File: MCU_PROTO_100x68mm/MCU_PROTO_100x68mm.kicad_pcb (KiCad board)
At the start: 2 copper layers, 90 x 58 mm, 251 parts, among them J1 Screw_Terminal_01x03, J10 Conn_01x01_Male, J2 Screw_Terminal_01x03, J3 Conn_01x20_Female, J4 Conn_01x20_Female, J5 Conn_01x20_Female, J6 Conn_01x20_Female, J7 Conn_01x20_Female, J8 Conn_01x20_Female, J9 Conn_01x01_Male

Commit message: pads in process
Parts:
- removed the REF** at (157.5, 143.6)
- removed the REF** at (134.7, 143.6)
- removed the REF** at (139.7, 118.2)
- removed the REF** at (137.2, 118.2)
- removed the REF** at (134.7, 118.2)
- removed the REF** at (132.1, 118.2)
- removed the REF** at (129.6, 118.2)
- removed the REF** at (127.0, 118.2)
- removed the REF** at (124.5, 118.2)
- removed the REF** at (122.0, 118.2)
- removed the REF** at (119.4, 118.2)
- removed the REF** at (116.9, 118.2)
- removed the REF** at (132.1, 143.6)
- removed the REF** at (114.3, 118.2)
- removed the REF** at (111.8, 118.2)
- removed the REF** at (109.3, 118.2)
- removed the REF** at (157.5, 115.6)
- removed the REF** at (155.0, 115.6)
- removed the REF** at (152.4, 115.6)
- removed the REF** at (149.9, 115.6)
- removed the REF** at (147.4, 115.6)
- removed the REF** at (144.8, 115.6)
- removed the REF** at (142.3, 115.6)
- removed the REF** at (129.6, 143.6)
- removed the REF** at (139.7, 115.6)
- removed the REF** at (137.2, 115.6)
- removed the REF** at (134.7, 115.6)
- removed the REF** at (132.1, 115.6)
- removed the REF** at (129.6, 115.6)
- removed the REF** at (127.0, 115.6)
- removed the REF** at (124.5, 115.6)
- removed the REF** at (122.0, 115.6)
- removed the REF** at (119.4, 115.6)
- removed the REF** at (116.9, 115.6)
- removed the REF** at (127.0, 143.6)
- removed the REF** at (114.3, 115.6)
- removed the REF** at (111.8, 115.6)
- removed the REF** at (109.3, 115.6)
- removed the REF** at (157.5, 113.1)
- removed the REF** at (155.0, 113.1)
- removed the REF** at (152.4, 113.1)
- removed the REF** at (149.9, 113.1)
- removed the REF** at (147.4, 113.1)
- removed the REF** at (144.8, 113.1)
- removed the REF** at (142.3, 113.1)
- removed the REF** at (124.5, 143.6)
- removed the REF** at (139.7, 113.1)
- removed the REF** at (137.2, 113.1)
- removed the REF** at (134.7, 113.1)
- removed the REF** at (132.1, 113.1)
- removed the REF** at (129.6, 113.1)
- removed the REF** at (127.0, 113.1)
- removed the REF** at (124.5, 113.1)
- removed the REF** at (122.0, 113.1)
- removed the REF** at (119.4, 113.1)
- removed the REF** at (116.9, 113.1)
- removed the REF** at (122.0, 143.6)
- removed the REF** at (114.3, 113.1)
- removed the REF** at (111.8, 113.1)
- removed the REF** at (109.3, 113.1)
- removed the REF** at (157.5, 110.5)
- removed the REF** at (155.0, 110.5)
- removed the REF** at (152.4, 110.5)
- removed the REF** at (149.9, 110.5)
- removed the REF** at (147.4, 110.5)
- removed the REF** at (144.8, 110.5)
- removed the REF** at (142.3, 110.5)
- removed the REF** at (119.4, 143.6)
- removed the REF** at (139.7, 110.5)
- removed the REF** at (137.2, 110.5)
- removed the REF** at (134.7, 110.5)
- removed the REF** at (132.1, 110.5)
- removed the REF** at (129.6, 110.5)
- removed the REF** at (127.0, 110.5)
- removed the REF** at (124.5, 110.5)
- removed the REF** at (122.0, 110.5)
- removed the REF** at (119.4, 110.5)
- removed the REF** at (116.9, 110.5)
- removed the REF** at (157.5, 141.0)
- removed the REF** at (114.3, 110.5)
- removed the REF** at (111.8, 110.5)
- removed the REF** at (109.3, 110.5)
- removed the REF** at (157.5, 108.0)
- removed the REF** at (155.0, 108.0)
- removed the REF** at (152.4, 108.0)
- removed the REF** at (149.9, 108.0)
- removed the REF** at (147.4, 108.0)
- removed the REF** at (144.8, 108.0)
- removed the REF** at (142.3, 108.0)
- removed the REF** at (155.0, 141.0)
- removed the REF** at (139.7, 108.0)
- removed the REF** at (137.2, 108.0)
- removed the REF** at (134.7, 108.0)
- removed the REF** at (132.1, 108.0)
- removed the REF** at (129.6, 108.0)
- removed the REF** at (127.0, 108.0)
- removed the REF** at (124.5, 108.0)
- removed the REF** at (122.0, 108.0)
- removed the REF** at (119.4, 108.0)
- removed the REF** at (116.9, 108.0)
- removed the REF** at (152.4, 141.0)
- removed the REF** at (114.3, 108.0)
- removed the REF** at (111.8, 108.0)
- removed the REF** at (122.0, 146.1)
- removed the REF** at (155.0, 143.6)
- removed the REF** at (149.9, 141.0)
- removed the REF** at (119.4, 146.1)
- removed the REF** at (157.5, 146.1)
- removed the REF** at (155.0, 146.1)
- removed the REF** at (137.2, 146.1)
- removed the REF** at (144.8, 146.1)
- removed the REF** at (139.7, 146.1)
- removed the REF** at (134.7, 146.1)
- removed the REF** at (132.1, 146.1)
- removed the REF** at (129.6, 146.1)
- removed the REF** at (127.0, 146.1)
- removed the REF** at (147.4, 141.0)
- removed the REF** at (124.5, 146.1)
- removed the REF** at (142.3, 146.1)
- removed the REF** at (147.4, 146.1)
- removed the REF** at (152.4, 146.1)
- removed the REF** at (149.9, 146.1)
- removed the REF** at (144.8, 141.0)
- removed the REF** at (160.1, 114.7)
- removed the REF** at (160.1, 137.8)
- removed the REF** at (160.1, 134.3)
- removed the REF** at (160.1, 130.8)
- removed the REF** at (160.1, 118.2)
- removed the REF** at (160.1, 111.2)
- removed the REF** at (142.3, 141.0)
- removed the REF** at (139.7, 141.0)
- removed the REF** at (137.2, 141.0)
- removed the REF** at (134.7, 141.0)
- removed the REF** at (132.1, 141.0)
- removed the REF** at (129.6, 141.0)
- removed the REF** at (127.0, 141.0)
- removed the REF** at (152.4, 143.6)
- removed the REF** at (124.5, 141.0)
- removed the REF** at (122.0, 141.0)
- removed the REF** at (119.4, 141.0)
- removed the REF** at (157.5, 138.5)
- removed the REF** at (155.0, 138.5)
- removed the REF** at (152.4, 138.5)
- removed the REF** at (149.9, 138.5)
- removed the REF** at (147.4, 138.5)
- removed the REF** at (144.8, 138.5)
- removed the REF** at (142.3, 138.5)
- removed the REF** at (149.9, 143.6)
- removed the REF** at (139.7, 138.5)
- removed the REF** at (137.2, 138.5)
- removed the REF** at (134.7, 138.5)
- removed the REF** at (132.1, 138.5)
- removed the REF** at (129.6, 138.5)
- removed the REF** at (127.0, 138.5)
- removed the REF** at (124.5, 138.5)
- removed the REF** at (122.0, 138.5)
- removed the REF** at (119.4, 138.5)
- removed the REF** at (116.9, 138.5)
- removed the REF** at (147.4, 143.6)
- removed the REF** at (114.3, 138.5)
- removed the REF** at (111.8, 138.5)
- removed the REF** at (109.3, 138.5)
- removed the REF** at (157.5, 135.9)
- removed the REF** at (155.0, 135.9)
- removed the REF** at (152.4, 135.9)
- removed the REF** at (149.9, 135.9)
- removed the REF** at (147.4, 135.9)
- removed the REF** at (144.8, 135.9)
- removed the REF** at (142.3, 135.9)
- removed the REF** at (144.8, 143.6)
- removed the REF** at (139.7, 135.9)
- removed the REF** at (137.2, 135.9)
- removed the REF** at (134.7, 135.9)
- removed the REF** at (132.1, 135.9)
- removed the REF** at (129.6, 135.9)
- removed the REF** at (127.0, 135.9)
- removed the REF** at (124.5, 135.9)
- removed the REF** at (122.0, 135.9)
- removed the REF** at (119.4, 135.9)
- removed the REF** at (116.9, 135.9)
- removed the REF** at (142.3, 143.6)
- removed the REF** at (114.3, 135.9)
- removed the REF** at (111.8, 135.9)
- removed the REF** at (157.5, 120.7)
- removed the REF** at (155.0, 120.7)
- removed the REF** at (152.4, 120.7)
- removed the REF** at (149.9, 120.7)
- removed the REF** at (147.4, 120.7)
- removed the REF** at (144.8, 120.7)
- removed the REF** at (142.3, 120.7)
- removed the REF** at (139.7, 143.6)
- removed the REF** at (139.7, 120.7)
- removed the REF** at (137.2, 120.7)
- removed the REF** at (134.7, 120.7)
- removed the REF** at (132.1, 120.7)
- removed the REF** at (129.6, 120.7)
- removed the REF** at (127.0, 120.7)
- removed the REF** at (124.5, 120.7)
- removed the REF** at (122.0, 120.7)
- removed the REF** at (119.4, 120.7)
- removed the REF** at (116.9, 120.7)
- removed the REF** at (137.2, 143.6)
- removed the REF** at (114.3, 120.7)
- removed the REF** at (111.8, 120.7)
- removed the REF** at (109.3, 120.7)
- removed the REF** at (157.5, 118.2)
- removed the REF** at (155.0, 118.2)
- removed the REF** at (152.4, 118.2)
- removed the REF** at (149.9, 118.2)
- removed the REF** at (147.4, 118.2)
- removed the REF** at (144.8, 118.2)
- removed the REF** at (142.3, 118.2)
- added REF**: SolderWirePad_1x01_Drill0.8mm, Connector_Wire:SolderWirePad_1x01_Drill0.8mm, F.Cu at (161.3, 146.1)
- added REF**: SolderWirePad_1x01_Drill0.8mm, Connector_Wire:SolderWirePad_1x01_Drill0.8mm, F.Cu at (138.4, 146.1)
- added REF**: SolderWirePad_1x01_Drill0.8mm, Connector_Wire:SolderWirePad_1x01_Drill0.8mm, F.Cu at (161.3, 120.7)
- added REF**: SolderWirePad_1x01_Drill0.8mm, Connector_Wire:SolderWirePad_1x01_Drill0.8mm, F.Cu at (158.7, 120.7)
- added REF**: SolderWirePad_1x01_Drill0.8mm, Connector_Wire:SolderWirePad_1x01_Drill0.8mm, F.Cu at (156.2, 120.7)
- added REF**: SolderWirePad_1x01_Drill0.8mm, Connector_Wire:SolderWirePad_1x01_Drill0.8mm, F.Cu at (153.6, 120.7)
- added REF**: SolderWirePad_1x01_Drill0.8mm, Connector_Wire:SolderWirePad_1x01_Drill0.8mm, F.Cu at (151.1, 120.7)
- added REF**: SolderWirePad_1x01_Drill0.8mm, Connector_Wire:SolderWirePad_1x01_Drill0.8mm, F.Cu at (148.6, 120.7)
- added REF**: SolderWirePad_1x01_Drill0.8mm, Connector_Wire:SolderWirePad_1x01_Drill0.8mm, F.Cu at (146.0, 120.7)
- added REF**: SolderWirePad_1x01_Drill0.8mm, Connector_Wire:SolderWirePad_1x01_Drill0.8mm, F.Cu at (143.5, 120.7)
- added REF**: SolderWirePad_1x01_Drill0.8mm, Connector_Wire:SolderWirePad_1x01_Drill0.8mm, F.Cu at (140.9, 120.7)
- added REF**: SolderWirePad_1x01_Drill0.8mm, Connector_Wire:SolderWirePad_1x01_Drill0.8mm, F.Cu at (138.4, 120.7)
- added REF**: SolderWirePad_1x01_Drill0.8mm, Connector_Wire:SolderWirePad_1x01_Drill0.8mm, F.Cu at (135.9, 146.1)
- added REF**: SolderWirePad_1x01_Drill0.8mm, Connector_Wire:SolderWirePad_1x01_Drill0.8mm, F.Cu at (135.9, 120.7)
- added REF**: SolderWirePad_1x01_Drill0.8mm, Connector_Wire:SolderWirePad_1x01_Drill0.8mm, F.Cu at (133.3, 120.7)
- added REF**: SolderWirePad_1x01_Drill0.8mm, Connector_Wire:SolderWirePad_1x01_Drill0.8mm, F.Cu at (130.8, 120.7)
- added REF**: SolderWirePad_1x01_Drill0.8mm, Connector_Wire:SolderWirePad_1x01_Drill0.8mm, F.Cu at (128.2, 120.7)
- added REF**: SolderWirePad_1x01_Drill0.8mm, Connector_Wire:SolderWirePad_1x01_Drill0.8mm, F.Cu at (125.7, 120.7)
- added REF**: SolderWirePad_1x01_Drill0.8mm, Connector_Wire:SolderWirePad_1x01_Drill0.8mm, F.Cu at (123.2, 120.7)
- added REF**: SolderWirePad_1x01_Drill0.8mm, Connector_Wire:SolderWirePad_1x01_Drill0.8mm, F.Cu at (120.6, 120.7)
- added REF**: SolderWirePad_1x01_Drill0.8mm, Connector_Wire:SolderWirePad_1x01_Drill0.8mm, F.Cu at (118.1, 120.7)
- added REF**: SolderWirePad_1x01_Drill0.8mm, Connector_Wire:SolderWirePad_1x01_Drill0.8mm, F.Cu at (115.5, 120.7)
- added REF**: SolderWirePad_1x01_Drill0.8mm, Connector_Wire:SolderWirePad_1x01_Drill0.8mm, F.Cu at (113.0, 120.7)
- added REF**: SolderWirePad_1x01_Drill0.8mm, Connector_Wire:SolderWirePad_1x01_Drill0.8mm, F.Cu at (133.3, 146.1)
- added REF**: SolderWirePad_1x01_Drill0.8mm, Connector_Wire:SolderWirePad_1x01_Drill0.8mm, F.Cu at (161.3, 118.2)
- added REF**: SolderWirePad_1x01_Drill0.8mm, Connector_Wire:SolderWirePad_1x01_Drill0.8mm, F.Cu at (158.7, 118.2)
- added REF**: SolderWirePad_1x01_Drill0.8mm, Connector_Wire:SolderWirePad_1x01_Drill0.8mm, F.Cu at (156.2, 118.2)
- added REF**: SolderWirePad_1x01_Drill0.8mm, Connector_Wire:SolderWirePad_1x01_Drill0.8mm, F.Cu at (153.6, 118.2)
- added REF**: SolderWirePad_1x01_Drill0.8mm, Connector_Wire:SolderWirePad_1x01_Drill0.8mm, F.Cu at (151.1, 118.2)
- added REF**: SolderWirePad_1x01_Drill0.8mm, Connector_Wire:SolderWirePad_1x01_Drill0.8mm, F.Cu at (148.6, 118.2)
- added REF**: SolderWirePad_1x01_Drill0.8mm, Connector_Wire:SolderWirePad_1x01_Drill0.8mm, F.Cu at (146.0, 118.2)
- added REF**: SolderWirePad_1x01_Drill0.8mm, Connector_Wire:SolderWirePad_1x01_Drill0.8mm, F.Cu at (143.5, 118.2)
- added REF**: SolderWirePad_1x01_Drill0.8mm, Connector_Wire:SolderWirePad_1x01_Drill0.8mm, F.Cu at (140.9, 118.2)
- added REF**: SolderWirePad_1x01_Drill0.8mm, Connector_Wire:SolderWirePad_1x01_Drill0.8mm, F.Cu at (138.4, 118.2)
- added REF**: SolderWirePad_1x01_Drill0.8mm, Connector_Wire:SolderWirePad_1x01_Drill0.8mm, F.Cu at (130.8, 146.1)
- added REF**: SolderWirePad_1x01_Drill0.8mm, Connector_Wire:SolderWirePad_1x01_Drill0.8mm, F.Cu at (135.9, 118.2)
- added REF**: SolderWirePad_1x01_Drill0.8mm, Connector_Wire:SolderWirePad_1x01_Drill0.8mm, F.Cu at (133.3, 118.2)
- added REF**: SolderWirePad_1x01_Drill0.8mm, Connector_Wire:SolderWirePad_1x01_Drill0.8mm, F.Cu at (130.8, 118.2)
- added REF**: SolderWirePad_1x01_Drill0.8mm, Connector_Wire:SolderWirePad_1x01_Drill0.8mm, F.Cu at (128.2, 118.2)
- added REF**: SolderWirePad_1x01_Drill0.8mm, Connector_Wire:SolderWirePad_1x01_Drill0.8mm, F.Cu at (125.7, 118.2)
- added REF**: SolderWirePad_1x01_Drill0.8mm, Connector_Wire:SolderWirePad_1x01_Drill0.8mm, F.Cu at (123.2, 118.2)
- added REF**: SolderWirePad_1x01_Drill0.8mm, Connector_Wire:SolderWirePad_1x01_Drill0.8mm, F.Cu at (120.6, 118.2)
- added REF**: SolderWirePad_1x01_Drill0.8mm, Connector_Wire:SolderWirePad_1x01_Drill0.8mm, F.Cu at (118.1, 118.2)
- added REF**: SolderWirePad_1x01_Drill0.8mm, Connector_Wire:SolderWirePad_1x01_Drill0.8mm, F.Cu at (115.5, 118.2)
- added REF**: SolderWirePad_1x01_Drill0.8mm, Connector_Wire:SolderWirePad_1x01_Drill0.8mm, F.Cu at (113.0, 118.2)
- added REF**: SolderWirePad_1x01_Drill0.8mm, Connector_Wire:SolderWirePad_1x01_Drill0.8mm, F.Cu at (128.2, 146.1)
- added REF**: SolderWirePad_1x01_Drill0.8mm, Connector_Wire:SolderWirePad_1x01_Drill0.8mm, F.Cu at (161.3, 115.6)
- added REF**: SolderWirePad_1x01_Drill0.8mm, Connector_Wire:SolderWirePad_1x01_Drill0.8mm, F.Cu at (158.7, 115.6)
- added REF**: SolderWirePad_1x01_Drill0.8mm, Connector_Wire:SolderWirePad_1x01_Drill0.8mm, F.Cu at (156.2, 115.6)
- added REF**: SolderWirePad_1x01_Drill0.8mm, Connector_Wire:SolderWirePad_1x01_Drill0.8mm, F.Cu at (153.6, 115.6)
- added REF**: SolderWirePad_1x01_Drill0.8mm, Connector_Wire:SolderWirePad_1x01_Drill0.8mm, F.Cu at (151.1, 115.6)
- added REF**: SolderWirePad_1x01_Drill0.8mm, Connector_Wire:SolderWirePad_1x01_Drill0.8mm, F.Cu at (148.6, 115.6)
- added REF**: SolderWirePad_1x01_Drill0.8mm, Connector_Wire:SolderWirePad_1x01_Drill0.8mm, F.Cu at (146.0, 115.6)
- added REF**: SolderWirePad_1x01_Drill0.8mm, Connector_Wire:SolderWirePad_1x01_Drill0.8mm, F.Cu at (143.5, 115.6)
- added REF**: SolderWirePad_1x01_Drill0.8mm, Connector_Wire:SolderWirePad_1x01_Drill0.8mm, F.Cu at (140.9, 115.6)
- added REF**: SolderWirePad_1x01_Drill0.8mm, Connector_Wire:SolderWirePad_1x01_Drill0.8mm, F.Cu at (138.4, 115.6)
- added REF**: SolderWirePad_1x01_Drill0.8mm, Connector_Wire:SolderWirePad_1x01_Drill0.8mm, F.Cu at (125.7, 146.1)
- added REF**: SolderWirePad_1x01_Drill0.8mm, Connector_Wire:SolderWirePad_1x01_Drill0.8mm, F.Cu at (135.9, 115.6)
- added REF**: SolderWirePad_1x01_Drill0.8mm, Connector_Wire:SolderWirePad_1x01_Drill0.8mm, F.Cu at (133.3, 115.6)
- added REF**: SolderWirePad_1x01_Drill0.8mm, Connector_Wire:SolderWirePad_1x01_Drill0.8mm, F.Cu at (130.8, 115.6)
- added REF**: SolderWirePad_1x01_Drill0.8mm, Connector_Wire:SolderWirePad_1x01_Drill0.8mm, F.Cu at (128.2, 115.6)
- added REF**: SolderWirePad_1x01_Drill0.8mm, Connector_Wire:SolderWirePad_1x01_Drill0.8mm, F.Cu at (125.7, 115.6)
- added REF**: SolderWirePad_1x01_Drill0.8mm, Connector_Wire:SolderWirePad_1x01_Drill0.8mm, F.Cu at (123.2, 115.6)
- added REF**: SolderWirePad_1x01_Drill0.8mm, Connector_Wire:SolderWirePad_1x01_Drill0.8mm, F.Cu at (120.6, 115.6)
- added REF**: SolderWirePad_1x01_Drill0.8mm, Connector_Wire:SolderWirePad_1x01_Drill0.8mm, F.Cu at (118.1, 115.6)
- added REF**: SolderWirePad_1x01_Drill0.8mm, Connector_Wire:SolderWirePad_1x01_Drill0.8mm, F.Cu at (115.5, 115.6)
- added REF**: SolderWirePad_1x01_Drill0.8mm, Connector_Wire:SolderWirePad_1x01_Drill0.8mm, F.Cu at (113.0, 115.6)
- added REF**: SolderWirePad_1x01_Drill0.8mm, Connector_Wire:SolderWirePad_1x01_Drill0.8mm, F.Cu at (123.2, 146.1)
- added REF**: SolderWirePad_1x01_Drill0.8mm, Connector_Wire:SolderWirePad_1x01_Drill0.8mm, F.Cu at (161.3, 113.1)
- added REF**: SolderWirePad_1x01_Drill0.8mm, Connector_Wire:SolderWirePad_1x01_Drill0.8mm, F.Cu at (158.7, 113.1)
- added REF**: SolderWirePad_1x01_Drill0.8mm, Connector_Wire:SolderWirePad_1x01_Drill0.8mm, F.Cu at (156.2, 113.1)
- added REF**: SolderWirePad_1x01_Drill0.8mm, Connector_Wire:SolderWirePad_1x01_Drill0.8mm, F.Cu at (153.6, 113.1)
- added REF**: SolderWirePad_1x01_Drill0.8mm, Connector_Wire:SolderWirePad_1x01_Drill0.8mm, F.Cu at (151.1, 113.1)
- added REF**: SolderWirePad_1x01_Drill0.8mm, Connector_Wire:SolderWirePad_1x01_Drill0.8mm, F.Cu at (148.6, 113.1)
- added REF**: SolderWirePad_1x01_Drill0.8mm, Connector_Wire:SolderWirePad_1x01_Drill0.8mm, F.Cu at (146.0, 113.1)
- added REF**: SolderWirePad_1x01_Drill0.8mm, Connector_Wire:SolderWirePad_1x01_Drill0.8mm, F.Cu at (143.5, 113.1)
- added REF**: SolderWirePad_1x01_Drill0.8mm, Connector_Wire:SolderWirePad_1x01_Drill0.8mm, F.Cu at (140.9, 113.1)
- added REF**: SolderWirePad_1x01_Drill0.8mm, Connector_Wire:SolderWirePad_1x01_Drill0.8mm, F.Cu at (138.4, 113.1)
- added REF**: SolderWirePad_1x01_Drill0.8mm, Connector_Wire:SolderWirePad_1x01_Drill0.8mm, F.Cu at (120.6, 146.1)
- added REF**: SolderWirePad_1x01_Drill0.8mm, Connector_Wire:SolderWirePad_1x01_Drill0.8mm, F.Cu at (135.9, 113.1)
- added REF**: SolderWirePad_1x01_Drill0.8mm, Connector_Wire:SolderWirePad_1x01_Drill0.8mm, F.Cu at (133.3, 113.1)
- added REF**: SolderWirePad_1x01_Drill0.8mm, Connector_Wire:SolderWirePad_1x01_Drill0.8mm, F.Cu at (130.8, 113.1)
- added REF**: SolderWirePad_1x01_Drill0.8mm, Connector_Wire:SolderWirePad_1x01_Drill0.8mm, F.Cu at (128.2, 113.1)
- added REF**: SolderWirePad_1x01_Drill0.8mm, Connector_Wire:SolderWirePad_1x01_Drill0.8mm, F.Cu at (125.7, 113.1)
- added REF**: SolderWirePad_1x01_Drill0.8mm, Connector_Wire:SolderWirePad_1x01_Drill0.8mm, F.Cu at (123.2, 113.1)
- added REF**: SolderWirePad_1x01_Drill0.8mm, Connector_Wire:SolderWirePad_1x01_Drill0.8mm, F.Cu at (120.6, 113.1)
- added REF**: SolderWirePad_1x01_Drill0.8mm, Connector_Wire:SolderWirePad_1x01_Drill0.8mm, F.Cu at (118.1, 113.1)
- added REF**: SolderWirePad_1x01_Drill0.8mm, Connector_Wire:SolderWirePad_1x01_Drill0.8mm, F.Cu at (115.5, 113.1)
- added REF**: SolderWirePad_1x01_Drill0.8mm, Connector_Wire:SolderWirePad_1x01_Drill0.8mm, F.Cu at (113.0, 113.1)
- added REF**: SolderWirePad_1x01_Drill0.8mm, Connector_Wire:SolderWirePad_1x01_Drill0.8mm, F.Cu at (118.1, 146.1)
- added REF**: SolderWirePad_1x01_Drill0.8mm, Connector_Wire:SolderWirePad_1x01_Drill0.8mm, F.Cu at (161.3, 110.5)
- added REF**: SolderWirePad_1x01_Drill0.8mm, Connector_Wire:SolderWirePad_1x01_Drill0.8mm, F.Cu at (158.7, 110.5)
- added REF**: SolderWirePad_1x01_Drill0.8mm, Connector_Wire:SolderWirePad_1x01_Drill0.8mm, F.Cu at (156.2, 110.5)
- added REF**: SolderWirePad_1x01_Drill0.8mm, Connector_Wire:SolderWirePad_1x01_Drill0.8mm, F.Cu at (153.6, 110.5)
- added REF**: SolderWirePad_1x01_Drill0.8mm, Connector_Wire:SolderWirePad_1x01_Drill0.8mm, F.Cu at (151.1, 110.5)
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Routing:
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
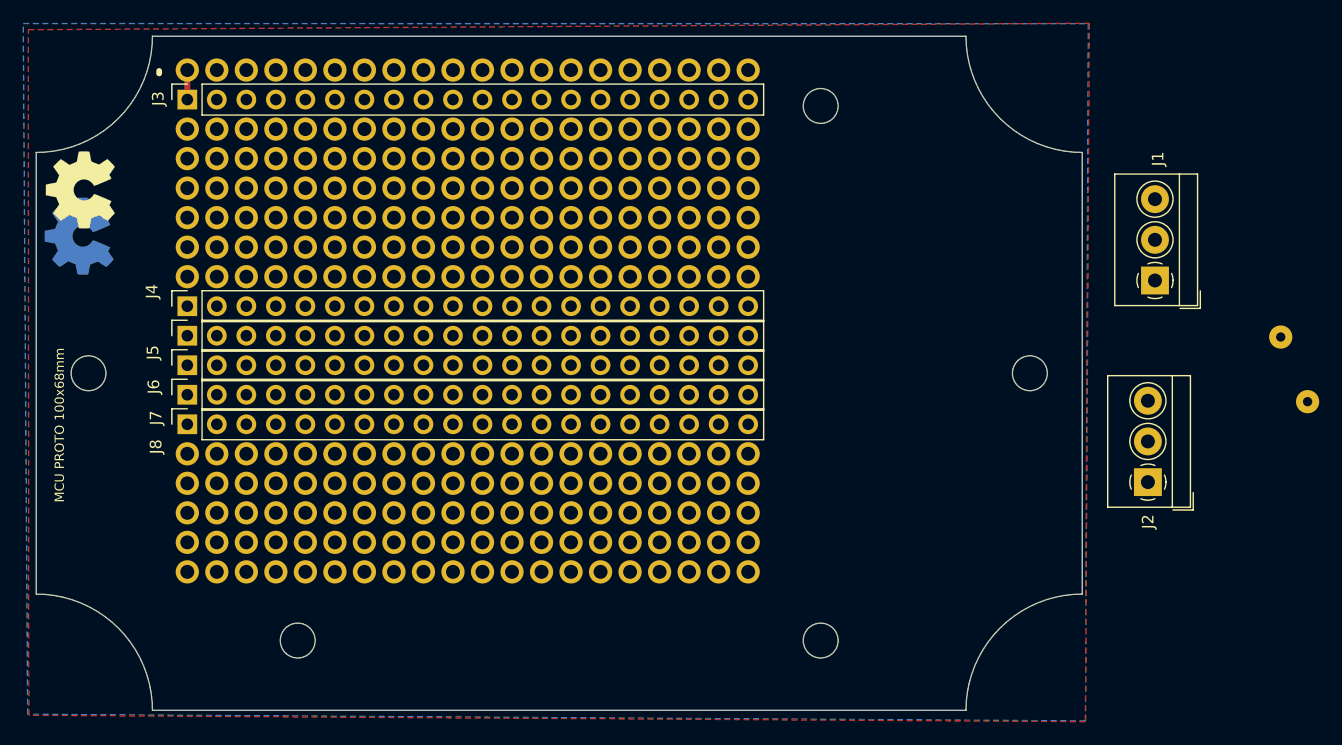
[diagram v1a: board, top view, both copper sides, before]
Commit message: adjusted drill distance
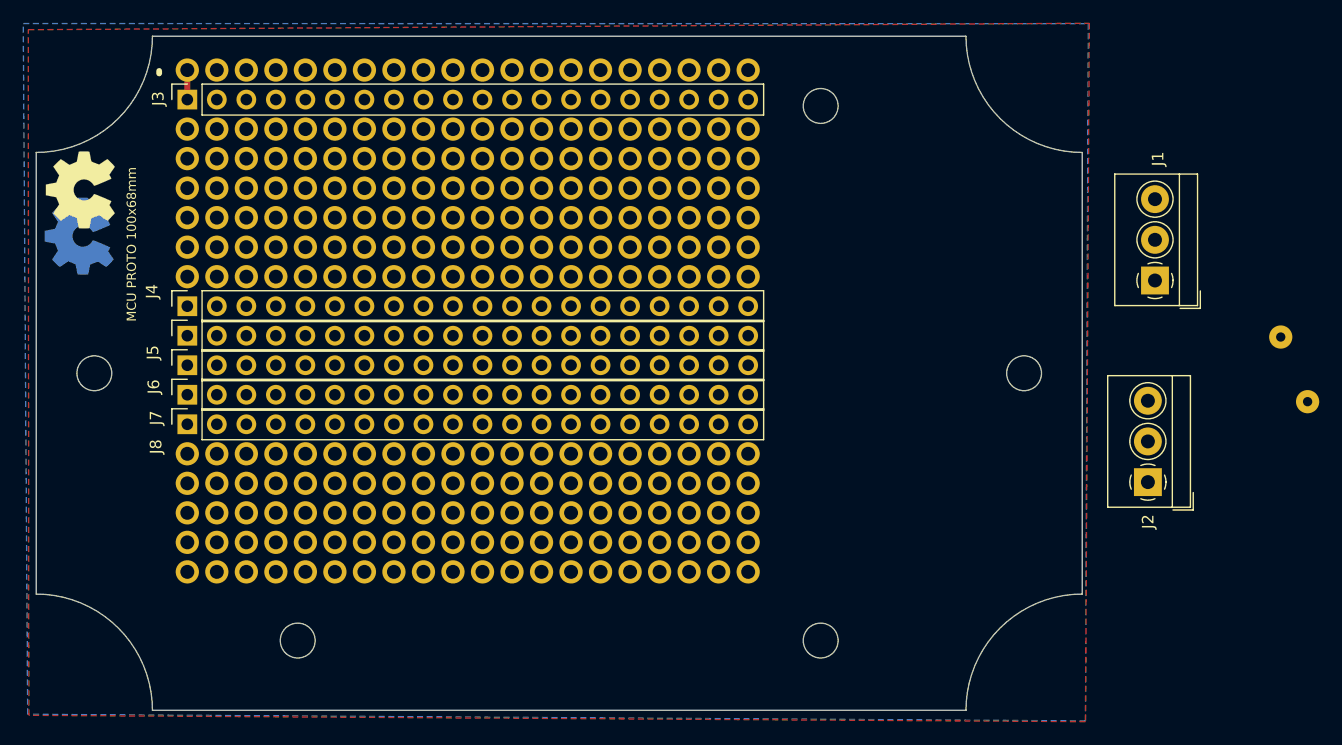
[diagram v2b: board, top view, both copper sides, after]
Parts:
- moved H2 0.50 mm to (105.0, 129.0)
- moved H5 0.50 mm to (185.0, 129.0)
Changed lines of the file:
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@@
   )
   (module MountingHole:MountingHole_3mm (layer F.Cu)
-    (at 104.5 129)
+    (at 105 129)
     (descr "Mounting Hole 3mm, no annular")
     (tags "mounting hole 3mm no annular")
@@
   )
   (module MountingHole:MountingHole_3mm (layer F.Cu)
-    (at 185.5 129)
+    (at 185 129)
     (descr "Mounting Hole 3mm, no annular")
     (tags "mounting hole 3mm no annular")
@@
   )
   (gr_line (start 110.5789 102.9843) (end 110.5789 103.2002) (layer F.SilkS) (width 0.5))
-  (gr_text "MCU PROTO 100x68mm" (at 103.9749 134.6327 90) (layer B.SilkS)
+  (gr_text "MCU PROTO 100x68mm" (at 108.4072 142.0114 90) (layer B.SilkS)
     (effects (font (size 0.8 0.8) (thickness 0.15)) (justify mirror))
   )
-  (gr_text "MCU PROTO 100x68mm\n\n" (at 102.6541 133.4643 90) (layer F.SilkS)
+  (gr_text "MCU PROTO 100x68mm\n\n" (at 108.8517 117.9068 90) (layer F.SilkS)
     (effects (font (size 0.8 0.8) (thickness 0.15)))
   )

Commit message: all pads placed
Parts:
- removed the REF** at (161.3, 110.5)
- removed the REF** at (158.7, 110.5)
- removed the REF** at (156.2, 110.5)
- removed the REF** at (153.6, 110.5)
- removed the REF** at (151.1, 110.5)
- removed the REF** at (148.6, 110.5)
- removed the REF** at (146.0, 110.5)
- removed the REF** at (143.5, 110.5)
- removed the REF** at (140.9, 110.5)
- removed the REF** at (138.4, 110.5)
- removed the REF** at (135.9, 110.5)
- removed the REF** at (133.3, 110.5)
- removed the REF** at (130.8, 110.5)
- removed the REF** at (128.2, 110.5)
- removed the REF** at (125.7, 110.5)
- removed the REF** at (123.2, 110.5)
- removed the REF** at (120.6, 110.5)
- removed the REF** at (118.1, 110.5)
- removed the REF** at (115.5, 110.5)
- removed the REF** at (113.0, 110.5)
- removed the REF** at (161.3, 108.0)
- removed the REF** at (158.7, 108.0)
- removed the REF** at (156.2, 108.0)
- removed the REF** at (153.6, 108.0)
- removed the REF** at (151.1, 108.0)
- removed the REF** at (148.6, 108.0)
- removed the REF** at (146.0, 108.0)
- removed the REF** at (143.5, 108.0)
- removed the REF** at (140.9, 108.0)
- removed the REF** at (138.4, 108.0)
- removed the REF** at (135.9, 108.0)
- removed the REF** at (133.3, 108.0)
- removed the REF** at (130.8, 108.0)
- removed the REF** at (128.2, 108.0)
- removed the REF** at (125.7, 108.0)
- removed the REF** at (123.2, 108.0)
- removed the REF** at (120.6, 108.0)
- removed the REF** at (118.1, 108.0)
- removed the REF** at (115.5, 108.0)
- removed the REF** at (113.0, 108.0)
- added J4: Conn_01x20_Female, Connector_PinSocket_2.54mm:PinSocket_1x20_P2.54mm_Vertical, F.Cu at (113.0, 108.0)
- added J5: Conn_01x20_Female, Connector_PinSocket_2.54mm:PinSocket_1x20_P2.54mm_Vertical, F.Cu at (113.0, 110.5)
- added REF**: SolderWirePad_1x01_Drill0.8mm, Connector_Wire:SolderWirePad_1x01_Drill0.8mm, F.Cu at (174.5, 121.5)
- added REF**: SolderWirePad_1x01_Drill0.8mm, Connector_Wire:SolderWirePad_1x01_Drill0.8mm, F.Cu at (163.8, 130.8)
- added REF**: SolderWirePad_1x01_Drill0.8mm, Connector_Wire:SolderWirePad_1x01_Drill0.8mm, F.Cu at (143.5, 148.6)
- added REF**: SolderWirePad_1x01_Drill0.8mm, Connector_Wire:SolderWirePad_1x01_Drill0.8mm, F.Cu at (140.9, 148.6)
- added REF**: SolderWirePad_1x01_Drill0.8mm, Connector_Wire:SolderWirePad_1x01_Drill0.8mm, F.Cu at (138.4, 148.6)
- added REF**: SolderWirePad_1x01_Drill0.8mm, Connector_Wire:SolderWirePad_1x01_Drill0.8mm, F.Cu at (135.9, 148.6)
- added REF**: SolderWirePad_1x01_Drill0.8mm, Connector_Wire:SolderWirePad_1x01_Drill0.8mm, F.Cu at (133.3, 148.6)
- added REF**: SolderWirePad_1x01_Drill0.8mm, Connector_Wire:SolderWirePad_1x01_Drill0.8mm, F.Cu at (130.8, 148.6)
- added REF**: SolderWirePad_1x01_Drill0.8mm, Connector_Wire:SolderWirePad_1x01_Drill0.8mm, F.Cu at (128.2, 148.6)
- added REF**: SolderWirePad_1x01_Drill0.8mm, Connector_Wire:SolderWirePad_1x01_Drill0.8mm, F.Cu at (115.5, 156.2)
- added REF**: SolderWirePad_1x01_Drill0.8mm, Connector_Wire:SolderWirePad_1x01_Drill0.8mm, F.Cu at (113.0, 156.2)
- added REF**: SolderWirePad_1x01_Drill0.8mm, Connector_Wire:SolderWirePad_1x01_Drill0.8mm, F.Cu at (115.5, 153.7)
- added REF**: SolderWirePad_1x01_Drill0.8mm, Connector_Wire:SolderWirePad_1x01_Drill0.8mm, F.Cu at (168.9, 128.3)
- added REF**: SolderWirePad_1x01_Drill0.8mm, Connector_Wire:SolderWirePad_1x01_Drill0.8mm, F.Cu at (113.0, 153.7)
- added REF**: SolderWirePad_1x01_Drill0.8mm, Connector_Wire:SolderWirePad_1x01_Drill0.8mm, F.Cu at (115.5, 151.2)
- added REF**: SolderWirePad_1x01_Drill0.8mm, Connector_Wire:SolderWirePad_1x01_Drill0.8mm, F.Cu at (113.0, 151.2)
- added REF**: SolderWirePad_1x01_Drill0.8mm, Connector_Wire:SolderWirePad_1x01_Drill0.8mm, F.Cu at (115.5, 148.6)
- added REF**: SolderWirePad_1x01_Drill0.8mm, Connector_Wire:SolderWirePad_1x01_Drill0.8mm, F.Cu at (113.0, 148.6)
- added REF**: SolderWirePad_1x01_Drill0.8mm, Connector_Wire:SolderWirePad_1x01_Drill0.8mm, F.Cu at (166.3, 128.3)
- added REF**: SolderWirePad_1x01_Drill0.8mm, Connector_Wire:SolderWirePad_1x01_Drill0.8mm, F.Cu at (163.8, 128.3)
- added REF**: SolderWirePad_1x01_Drill0.8mm, Connector_Wire:SolderWirePad_1x01_Drill0.8mm, F.Cu at (168.9, 125.8)
- added REF**: SolderWirePad_1x01_Drill0.8mm, Connector_Wire:SolderWirePad_1x01_Drill0.8mm, F.Cu at (166.3, 125.8)
- added REF**: SolderWirePad_1x01_Drill0.8mm, Connector_Wire:SolderWirePad_1x01_Drill0.8mm, F.Cu at (163.8, 125.8)
- added REF**: SolderWirePad_1x01_Drill0.8mm, Connector_Wire:SolderWirePad_1x01_Drill0.8mm, F.Cu at (168.9, 123.2)
- added REF**: SolderWirePad_1x01_Drill0.8mm, Connector_Wire:SolderWirePad_1x01_Drill0.8mm, F.Cu at (166.3, 123.2)
- added REF**: SolderWirePad_1x01_Drill0.8mm, Connector_Wire:SolderWirePad_1x01_Drill0.8mm, F.Cu at (163.8, 123.2)
- added REF**: SolderWirePad_1x01_Drill0.8mm, Connector_Wire:SolderWirePad_1x01_Drill0.8mm, F.Cu at (174.5, 118.0)
- added REF**: SolderWirePad_1x01_Drill0.8mm, Connector_Wire:SolderWirePad_1x01_Drill0.8mm, F.Cu at (168.9, 120.7)
- added REF**: SolderWirePad_1x01_Drill0.8mm, Connector_Wire:SolderWirePad_1x01_Drill0.8mm, F.Cu at (166.3, 120.7)
- added REF**: SolderWirePad_1x01_Drill0.8mm, Connector_Wire:SolderWirePad_1x01_Drill0.8mm, F.Cu at (163.8, 120.7)
- added REF**: SolderWirePad_1x01_Drill0.8mm, Connector_Wire:SolderWirePad_1x01_Drill0.8mm, F.Cu at (168.9, 118.2)
- added REF**: SolderWirePad_1x01_Drill0.8mm, Connector_Wire:SolderWirePad_1x01_Drill0.8mm, F.Cu at (166.3, 118.2)
- added REF**: SolderWirePad_1x01_Drill0.8mm, Connector_Wire:SolderWirePad_1x01_Drill0.8mm, F.Cu at (163.8, 118.2)
- added REF**: SolderWirePad_1x01_Drill0.8mm, Connector_Wire:SolderWirePad_1x01_Drill0.8mm, F.Cu at (168.9, 115.6)
- added REF**: SolderWirePad_1x01_Drill0.8mm, Connector_Wire:SolderWirePad_1x01_Drill0.8mm, F.Cu at (166.3, 115.6)
- added REF**: SolderWirePad_1x01_Drill0.8mm, Connector_Wire:SolderWirePad_1x01_Drill0.8mm, F.Cu at (163.8, 115.6)
- added REF**: SolderWirePad_1x01_Drill0.8mm, Connector_Wire:SolderWirePad_1x01_Drill0.8mm, F.Cu at (168.9, 113.1)
- added REF**: SolderWirePad_1x01_Drill0.8mm, Connector_Wire:SolderWirePad_1x01_Drill0.8mm, F.Cu at (174.5, 114.5)
- added REF**: SolderWirePad_1x01_Drill0.8mm, Connector_Wire:SolderWirePad_1x01_Drill0.8mm, F.Cu at (166.3, 113.1)
- added REF**: SolderWirePad_1x01_Drill0.8mm, Connector_Wire:SolderWirePad_1x01_Drill0.8mm, F.Cu at (163.8, 113.1)
- added REF**: SolderWirePad_1x01_Drill0.8mm, Connector_Wire:SolderWirePad_1x01_Drill0.8mm, F.Cu at (174.5, 147.0)
- added REF**: SolderWirePad_1x01_Drill0.8mm, Connector_Wire:SolderWirePad_1x01_Drill0.8mm, F.Cu at (168.9, 146.1)
- added REF**: SolderWirePad_1x01_Drill0.8mm, Connector_Wire:SolderWirePad_1x01_Drill0.8mm, F.Cu at (166.3, 146.1)
- added REF**: SolderWirePad_1x01_Drill0.8mm, Connector_Wire:SolderWirePad_1x01_Drill0.8mm, F.Cu at (163.8, 146.1)
- added REF**: SolderWirePad_1x01_Drill0.8mm, Connector_Wire:SolderWirePad_1x01_Drill0.8mm, F.Cu at (174.5, 143.5)
- added REF**: SolderWirePad_1x01_Drill0.8mm, Connector_Wire:SolderWirePad_1x01_Drill0.8mm, F.Cu at (168.9, 143.6)
- added REF**: SolderWirePad_1x01_Drill0.8mm, Connector_Wire:SolderWirePad_1x01_Drill0.8mm, F.Cu at (166.3, 143.6)
- added REF**: SolderWirePad_1x01_Drill0.8mm, Connector_Wire:SolderWirePad_1x01_Drill0.8mm, F.Cu at (163.8, 143.6)
- added REF**: SolderWirePad_1x01_Drill0.8mm, Connector_Wire:SolderWirePad_1x01_Drill0.8mm, F.Cu at (174.5, 111.0)
- added REF**: SolderWirePad_1x01_Drill0.8mm, Connector_Wire:SolderWirePad_1x01_Drill0.8mm, F.Cu at (174.5, 140.0)
- added REF**: SolderWirePad_1x01_Drill0.8mm, Connector_Wire:SolderWirePad_1x01_Drill0.8mm, F.Cu at (168.9, 141.0)
- added REF**: SolderWirePad_1x01_Drill0.8mm, Connector_Wire:SolderWirePad_1x01_Drill0.8mm, F.Cu at (166.3, 141.0)
- added REF**: SolderWirePad_1x01_Drill0.8mm, Connector_Wire:SolderWirePad_1x01_Drill0.8mm, F.Cu at (163.8, 141.0)
- added REF**: SolderWirePad_1x01_Drill0.8mm, Connector_Wire:SolderWirePad_1x01_Drill0.8mm, F.Cu at (174.5, 136.5)
- added REF**: SolderWirePad_1x01_Drill0.8mm, Connector_Wire:SolderWirePad_1x01_Drill0.8mm, F.Cu at (168.9, 138.5)
- added REF**: SolderWirePad_1x01_Drill0.8mm, Connector_Wire:SolderWirePad_1x01_Drill0.8mm, F.Cu at (166.3, 138.5)
- added REF**: SolderWirePad_1x01_Drill0.8mm, Connector_Wire:SolderWirePad_1x01_Drill0.8mm, F.Cu at (163.8, 138.5)
- added REF**: SolderWirePad_1x01_Drill0.8mm, Connector_Wire:SolderWirePad_1x01_Drill0.8mm, F.Cu at (168.9, 135.9)
- added REF**: SolderWirePad_1x01_Drill0.8mm, Connector_Wire:SolderWirePad_1x01_Drill0.8mm, F.Cu at (166.3, 135.9)
- added REF**: SolderWirePad_1x01_Drill0.8mm, Connector_Wire:SolderWirePad_1x01_Drill0.8mm, F.Cu at (168.9, 133.4)
- added REF**: SolderWirePad_1x01_Drill0.8mm, Connector_Wire:SolderWirePad_1x01_Drill0.8mm, F.Cu at (163.8, 135.9)
- added REF**: SolderWirePad_1x01_Drill0.8mm, Connector_Wire:SolderWirePad_1x01_Drill0.8mm, F.Cu at (161.3, 156.2)
- added REF**: SolderWirePad_1x01_Drill0.8mm, Connector_Wire:SolderWirePad_1x01_Drill0.8mm, F.Cu at (158.7, 156.2)
- added REF**: SolderWirePad_1x01_Drill0.8mm, Connector_Wire:SolderWirePad_1x01_Drill0.8mm, F.Cu at (156.2, 156.2)
- added REF**: SolderWirePad_1x01_Drill0.8mm, Connector_Wire:SolderWirePad_1x01_Drill0.8mm, F.Cu at (153.6, 156.2)
- added REF**: SolderWirePad_1x01_Drill0.8mm, Connector_Wire:SolderWirePad_1x01_Drill0.8mm, F.Cu at (151.1, 156.2)
- added REF**: SolderWirePad_1x01_Drill0.8mm, Connector_Wire:SolderWirePad_1x01_Drill0.8mm, F.Cu at (148.6, 156.2)
- added REF**: SolderWirePad_1x01_Drill0.8mm, Connector_Wire:SolderWirePad_1x01_Drill0.8mm, F.Cu at (146.0, 156.2)
- added REF**: SolderWirePad_1x01_Drill0.8mm, Connector_Wire:SolderWirePad_1x01_Drill0.8mm, F.Cu at (143.5, 156.2)
- added REF**: SolderWirePad_1x01_Drill0.8mm, Connector_Wire:SolderWirePad_1x01_Drill0.8mm, F.Cu at (140.9, 156.2)
- added REF**: SolderWirePad_1x01_Drill0.8mm, Connector_Wire:SolderWirePad_1x01_Drill0.8mm, F.Cu at (166.3, 133.4)
- added REF**: SolderWirePad_1x01_Drill0.8mm, Connector_Wire:SolderWirePad_1x01_Drill0.8mm, F.Cu at (138.4, 156.2)
- added REF**: SolderWirePad_1x01_Drill0.8mm, Connector_Wire:SolderWirePad_1x01_Drill0.8mm, F.Cu at (135.9, 156.2)
- added REF**: SolderWirePad_1x01_Drill0.8mm, Connector_Wire:SolderWirePad_1x01_Drill0.8mm, F.Cu at (133.3, 156.2)
- added REF**: SolderWirePad_1x01_Drill0.8mm, Connector_Wire:SolderWirePad_1x01_Drill0.8mm, F.Cu at (130.8, 156.2)
- added REF**: SolderWirePad_1x01_Drill0.8mm, Connector_Wire:SolderWirePad_1x01_Drill0.8mm, F.Cu at (128.2, 156.2)
- added REF**: SolderWirePad_1x01_Drill0.8mm, Connector_Wire:SolderWirePad_1x01_Drill0.8mm, F.Cu at (161.3, 153.7)
- added REF**: SolderWirePad_1x01_Drill0.8mm, Connector_Wire:SolderWirePad_1x01_Drill0.8mm, F.Cu at (158.7, 153.7)
- added REF**: SolderWirePad_1x01_Drill0.8mm, Connector_Wire:SolderWirePad_1x01_Drill0.8mm, F.Cu at (156.2, 153.7)
- added REF**: SolderWirePad_1x01_Drill0.8mm, Connector_Wire:SolderWirePad_1x01_Drill0.8mm, F.Cu at (153.6, 153.7)
- added REF**: SolderWirePad_1x01_Drill0.8mm, Connector_Wire:SolderWirePad_1x01_Drill0.8mm, F.Cu at (151.1, 153.7)
- added REF**: SolderWirePad_1x01_Drill0.8mm, Connector_Wire:SolderWirePad_1x01_Drill0.8mm, F.Cu at (163.8, 133.4)
- added REF**: SolderWirePad_1x01_Drill0.8mm, Connector_Wire:SolderWirePad_1x01_Drill0.8mm, F.Cu at (148.6, 153.7)
- added REF**: SolderWirePad_1x01_Drill0.8mm, Connector_Wire:SolderWirePad_1x01_Drill0.8mm, F.Cu at (146.0, 153.7)
- added REF**: SolderWirePad_1x01_Drill0.8mm, Connector_Wire:SolderWirePad_1x01_Drill0.8mm, F.Cu at (143.5, 153.7)
- added REF**: SolderWirePad_1x01_Drill0.8mm, Connector_Wire:SolderWirePad_1x01_Drill0.8mm, F.Cu at (140.9, 153.7)
- added REF**: SolderWirePad_1x01_Drill0.8mm, Connector_Wire:SolderWirePad_1x01_Drill0.8mm, F.Cu at (138.4, 153.7)
- added REF**: SolderWirePad_1x01_Drill0.8mm, Connector_Wire:SolderWirePad_1x01_Drill0.8mm, F.Cu at (135.9, 153.7)
- added REF**: SolderWirePad_1x01_Drill0.8mm, Connector_Wire:SolderWirePad_1x01_Drill0.8mm, F.Cu at (133.3, 153.7)
- added REF**: SolderWirePad_1x01_Drill0.8mm, Connector_Wire:SolderWirePad_1x01_Drill0.8mm, F.Cu at (130.8, 153.7)
- added REF**: SolderWirePad_1x01_Drill0.8mm, Connector_Wire:SolderWirePad_1x01_Drill0.8mm, F.Cu at (128.2, 153.7)
- added REF**: SolderWirePad_1x01_Drill0.8mm, Connector_Wire:SolderWirePad_1x01_Drill0.8mm, F.Cu at (161.3, 151.2)
- added REF**: SolderWirePad_1x01_Drill0.8mm, Connector_Wire:SolderWirePad_1x01_Drill0.8mm, F.Cu at (168.9, 130.8)
- added REF**: SolderWirePad_1x01_Drill0.8mm, Connector_Wire:SolderWirePad_1x01_Drill0.8mm, F.Cu at (158.7, 151.2)
- added REF**: SolderWirePad_1x01_Drill0.8mm, Connector_Wire:SolderWirePad_1x01_Drill0.8mm, F.Cu at (156.2, 151.2)
- added REF**: SolderWirePad_1x01_Drill0.8mm, Connector_Wire:SolderWirePad_1x01_Drill0.8mm, F.Cu at (153.6, 151.2)
- added REF**: SolderWirePad_1x01_Drill0.8mm, Connector_Wire:SolderWirePad_1x01_Drill0.8mm, F.Cu at (151.1, 151.2)
- added REF**: SolderWirePad_1x01_Drill0.8mm, Connector_Wire:SolderWirePad_1x01_Drill0.8mm, F.Cu at (148.6, 151.2)
- added REF**: SolderWirePad_1x01_Drill0.8mm, Connector_Wire:SolderWirePad_1x01_Drill0.8mm, F.Cu at (146.0, 151.2)
- added REF**: SolderWirePad_1x01_Drill0.8mm, Connector_Wire:SolderWirePad_1x01_Drill0.8mm, F.Cu at (143.5, 151.2)
- added REF**: SolderWirePad_1x01_Drill0.8mm, Connector_Wire:SolderWirePad_1x01_Drill0.8mm, F.Cu at (140.9, 151.2)
- added REF**: SolderWirePad_1x01_Drill0.8mm, Connector_Wire:SolderWirePad_1x01_Drill0.8mm, F.Cu at (138.4, 151.2)
- added REF**: SolderWirePad_1x01_Drill0.8mm, Connector_Wire:SolderWirePad_1x01_Drill0.8mm, F.Cu at (135.9, 151.2)
- added REF**: SolderWirePad_1x01_Drill0.8mm, Connector_Wire:SolderWirePad_1x01_Drill0.8mm, F.Cu at (166.3, 130.8)
- added REF**: SolderWirePad_1x01_Drill0.8mm, Connector_Wire:SolderWirePad_1x01_Drill0.8mm, F.Cu at (133.3, 151.2)
- added REF**: SolderWirePad_1x01_Drill0.8mm, Connector_Wire:SolderWirePad_1x01_Drill0.8mm, F.Cu at (130.8, 151.2)
- added REF**: SolderWirePad_1x01_Drill0.8mm, Connector_Wire:SolderWirePad_1x01_Drill0.8mm, F.Cu at (128.2, 151.2)
- added REF**: SolderWirePad_1x01_Drill0.8mm, Connector_Wire:SolderWirePad_1x01_Drill0.8mm, F.Cu at (161.3, 148.6)
- added REF**: SolderWirePad_1x01_Drill0.8mm, Connector_Wire:SolderWirePad_1x01_Drill0.8mm, F.Cu at (158.7, 148.6)
- added REF**: SolderWirePad_1x01_Drill0.8mm, Connector_Wire:SolderWirePad_1x01_Drill0.8mm, F.Cu at (156.2, 148.6)
- added REF**: SolderWirePad_1x01_Drill0.8mm, Connector_Wire:SolderWirePad_1x01_Drill0.8mm, F.Cu at (153.6, 148.6)
- added REF**: SolderWirePad_1x01_Drill0.8mm, Connector_Wire:SolderWirePad_1x01_Drill0.8mm, F.Cu at (151.1, 148.6)
- added REF**: SolderWirePad_1x01_Drill0.8mm, Connector_Wire:SolderWirePad_1x01_Drill0.8mm, F.Cu at (148.6, 148.6)
- added REF**: SolderWirePad_1x01_Drill0.8mm, Connector_Wire:SolderWirePad_1x01_Drill0.8mm, F.Cu at (146.0, 148.6)
- J1, J2: value Screw_Terminal_01x03 -> Screw_Terminal_01x04; footprint TerminalBlock_4Ucon:TerminalBlock_4Ucon_1x03_P3.50mm_Horizontal -> TerminalBlock_4Ucon:TerminalBlock_4Ucon_1x04_P3.50mm_Horizontal
- moved J12 34.9 mm to (174.5, 130.8)
- moved J11 32.7 mm to (174.5, 128.3)
- moved J2 17.9 mm to (180.0, 147.0)
- moved J1 16.3 mm to (180.0, 121.5)
- moved REF** 1.43 mm to (104.3, 114.6)
- moved REF** 0.72 mm to (104.4, 117.4)
- renumbered J8 to J10, J9 to J11, J10 to J12, J4 to J6, J5 to J7, J6 to J8, J7 to J9
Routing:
- net Net-(J2-Pad4): track 0.00 -> 11.3 mm
- net Net-(J2-Pad2): track 0.00 -> 11.2 mm
- net Net-(J1-Pad4): track 0.00 -> 11.2 mm
- net Net-(J1-Pad2): track 0.00 -> 10.9 mm
- net Net-(J1-Pad1): track 0.00 -> 10.9 mm
- net Net-(J2-Pad3): track 0.00 -> 10.8 mm
- net Net-(J2-Pad1): track 0.00 -> 10.6 mm
- net Net-(J1-Pad3): track 0.00 -> 10.2 mm
- net Net-(J3-Pad14): track 0.00 -> 5.29 mm
- net Net-(J3-Pad8): track 0.00 -> 5.24 mm
- net Net-(J3-Pad18): track 0.00 -> 5.17 mm
- net Net-(J3-Pad13): track 0.00 -> 5.12 mm
- net Net-(J3-Pad12): track 0.00 -> 5.10 mm
- net (no net): track 0.00 -> 5.08 mm
- net Net-(J3-Pad11): track 0.00 -> 5.05 mm
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
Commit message: some silks added
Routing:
- net (no net): track 5.08 -> 879.4 mm
- net Net-(J10-Pad17): track 0.00 -> 9.03 mm
- net Net-(J10-Pad6): track 0.00 -> 7.81 mm
- net Net-(J10-Pad10): track 0.00 -> 7.44 mm
- net Net-(J10-Pad2): track 0.00 -> 7.43 mm
- net Net-(J10-Pad14): track 0.00 -> 7.35 mm
- net Net-(J10-Pad18): track 0.00 -> 7.33 mm
- net Net-(J10-Pad7): track 0.00 -> 7.30 mm
- net Net-(J10-Pad5): track 0.00 -> 7.28 mm
- net Net-(J10-Pad20): track 0.00 -> 7.25 mm
- net Net-(J10-Pad9): track 0.00 -> 7.23 mm
- net Net-(J10-Pad3): track 0.00 -> 7.23 mm
- net Net-(J10-Pad4): track 0.00 -> 7.22 mm
- net Net-(J10-Pad15): track 0.00 -> 7.18 mm
- net Net-(J10-Pad8): track 0.00 -> 7.15 mm
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
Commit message: all silks finished
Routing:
- net (no net): track 879.4 -> 889.5 mm
